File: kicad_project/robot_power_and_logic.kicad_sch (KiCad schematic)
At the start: 17 parts

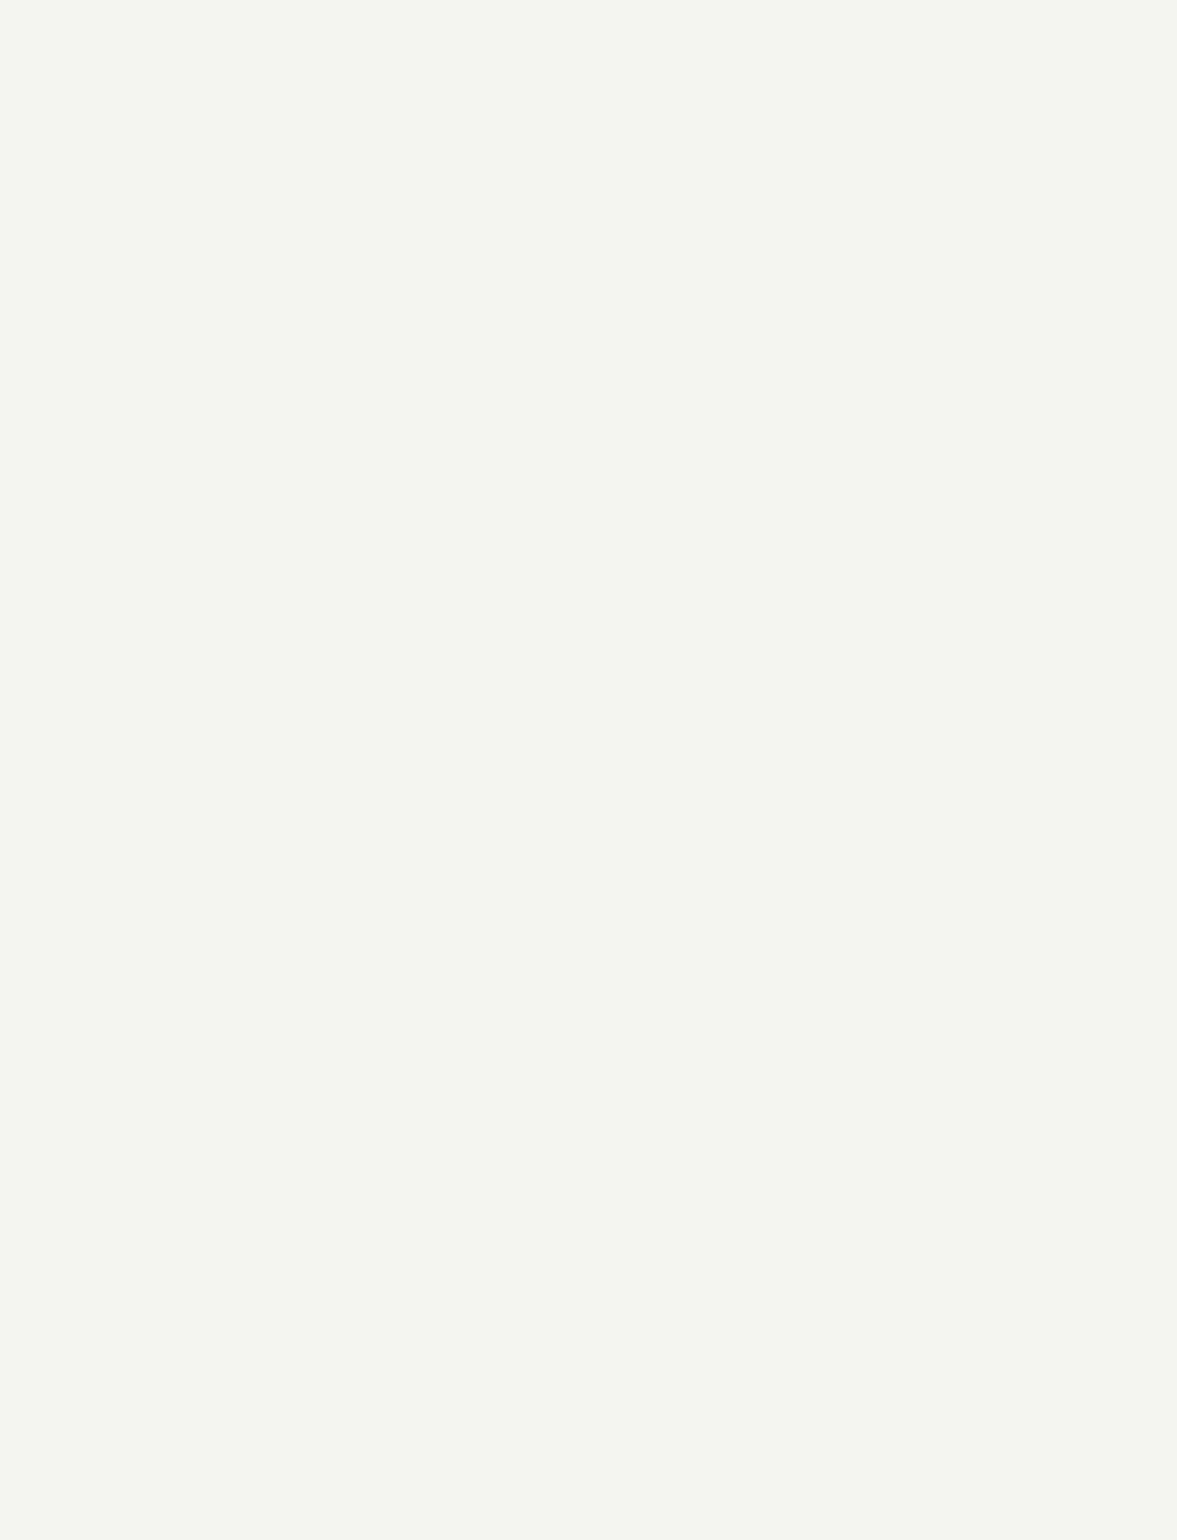
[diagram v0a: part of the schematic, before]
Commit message: Add 2nd motor driver
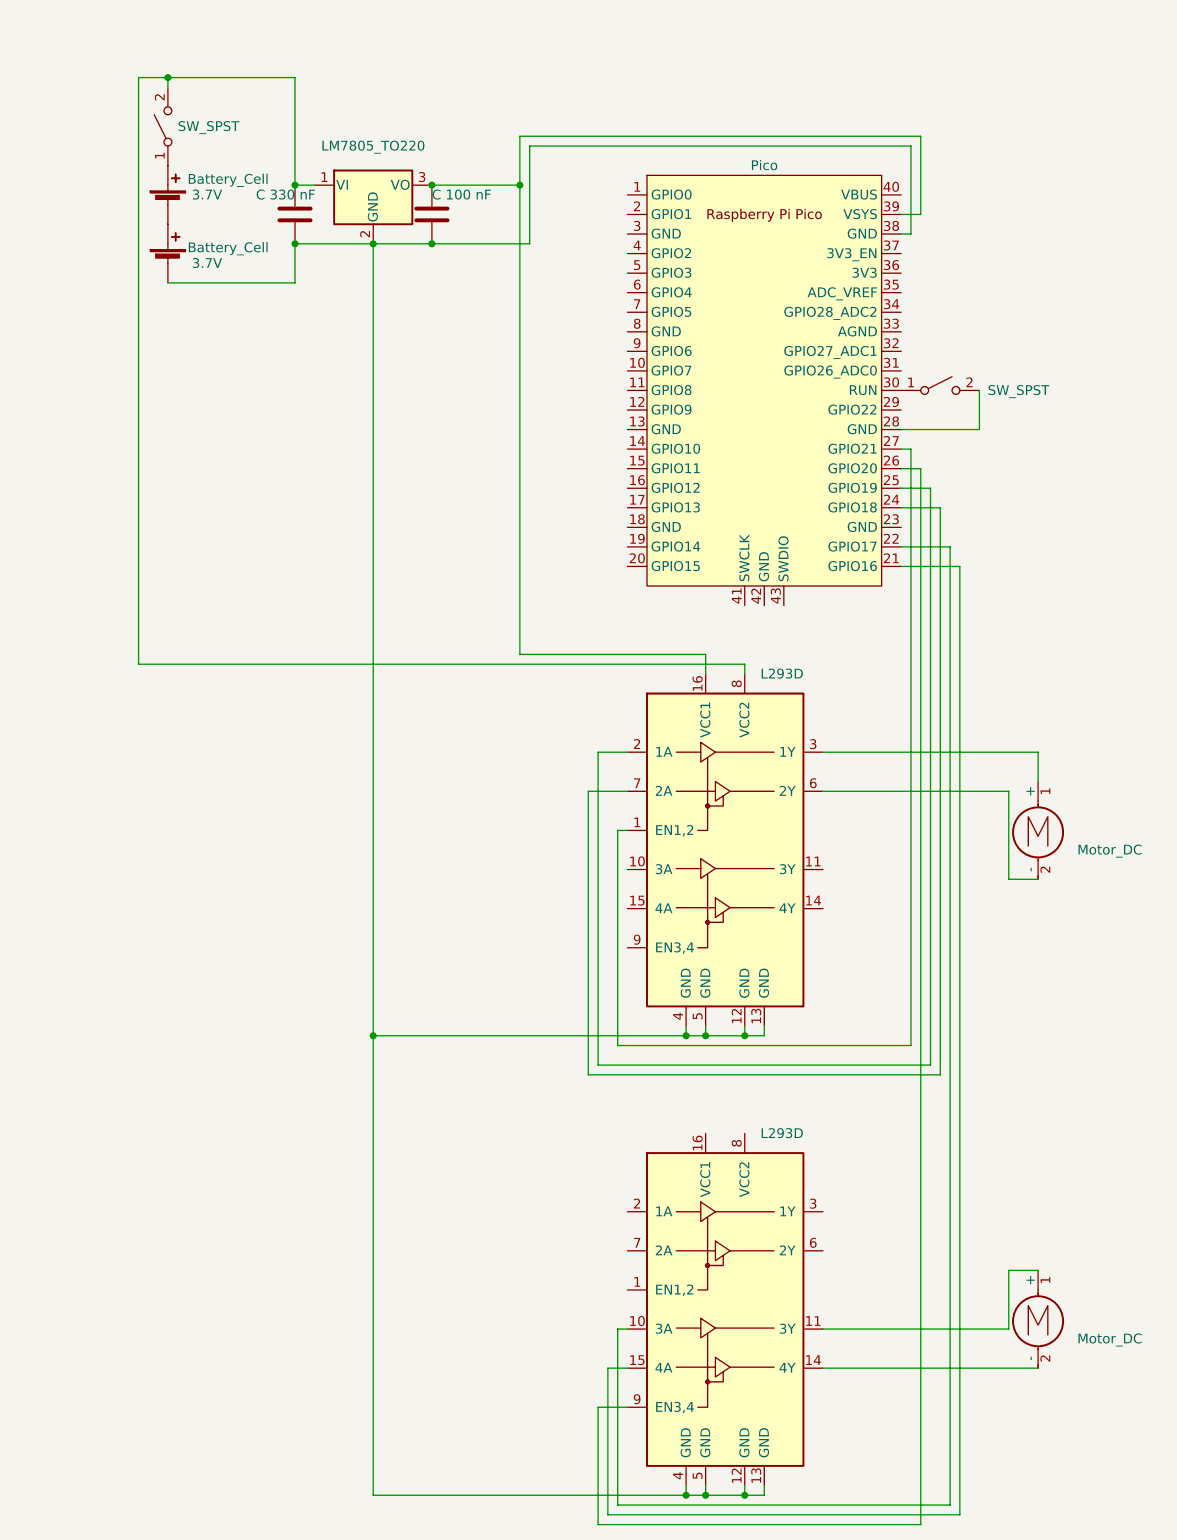
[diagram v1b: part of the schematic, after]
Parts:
- added BT? (x2): Battery_Cell, symbol Device:Battery_Cell
- added C?: C 330 nF, symbol Device:C
- added C?: C 100 nF, symbol Device:C
- added M? (x2): Motor_DC, symbol Motor:Motor_DC
- added SW? (x2): SW_SPST, symbol Switch:SW_SPST
- added U? (x2): L293D, Package_DIP:DIP-16_W7.62mm, symbol Driver_Motor:L293D
- added U?: LM7805_TO220, Package_TO_SOT_THT:TO-220-3_Vertical, symbol Regulator_Linear:LM7805_TO220
- added U?: Pico, RPi_Pico:RPi_Pico_SMD_TH, symbol MCU_RaspberryPi_and_Boards:Pico
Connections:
- new net: BT?.1 (+), SW?.1 (A)
- new net: C?.1, SW?.2 (B), U?.1 (VI), U?.8 (VCC2)
- new net: BT?.1 (+), BT?.2 (-)
- new net: BT?.2 (-), C?.2, C?.2, U?.12 (GND), U?.12 (GND), U?.13 (GND), U?.13 (GND), U?.2 (GND), U?.38 (GND), U?.4 (GND), U?.4 (GND), U?.5 (GND), U?.5 (GND)
- new net: U?.1 (EN1,2), U?.27 (GPIO21)
- new net: C?.1, U?.16 (VCC1), U?.3 (VO), U?.39 (VSYS)
- new net: U?.2 (1A), U?.25 (GPIO19)
- new net: M?.1 (+), U?.3 (1Y)
- new net: M?.2 (-), U?.6 (2Y)
- new net: U?.24 (GPIO18), U?.7 (2A)
- new net: U?.10 (3A), U?.22 (GPIO17)
- new net: M?.1 (+), U?.11 (3Y)
- new net: M?.2 (-), U?.14 (4Y)
- new net: U?.15 (4A), U?.21 (GPIO16)
- new net: U?.26 (GPIO20), U?.9 (EN3,4)
- new net: SW?.2 (B), U?.28 (GND)
- new net: SW?.1 (A), U?.30 (RUN)

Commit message: Remove previous circuit diagrams
cause we have version control for keeping them.
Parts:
- removed BT? (x2): Battery, symbol Device:Battery
- removed C?: C 100 nF, symbol Device:C
- removed C?: C 330 nF, symbol Device:C
- removed M? (x4): Motor_DC, symbol Motor:Motor_DC
- removed SW? (x3): SW_SPST, symbol Switch:SW_SPST
- removed U?: LM7805_TO220, Package_TO_SOT_THT:TO-220-3_Vertical, symbol Regulator_Linear:LM7805_TO220
- removed U? (x2): L293D, Package_DIP:DIP-16_W7.62mm, symbol Driver_Motor:L293D
- removed U?: LM2596T-ADJ, Package_TO_SOT_THT:TO-220-5_P3.4x3.7mm_StaggerOdd_Lead3.8mm_Vertical, symbol Regulator_Switching:LM2596T-ADJ
- removed U? (x2): Pico, RPi_Pico:RPi_Pico_SMD_TH, symbol MCU_RaspberryPi_and_Boards:Pico

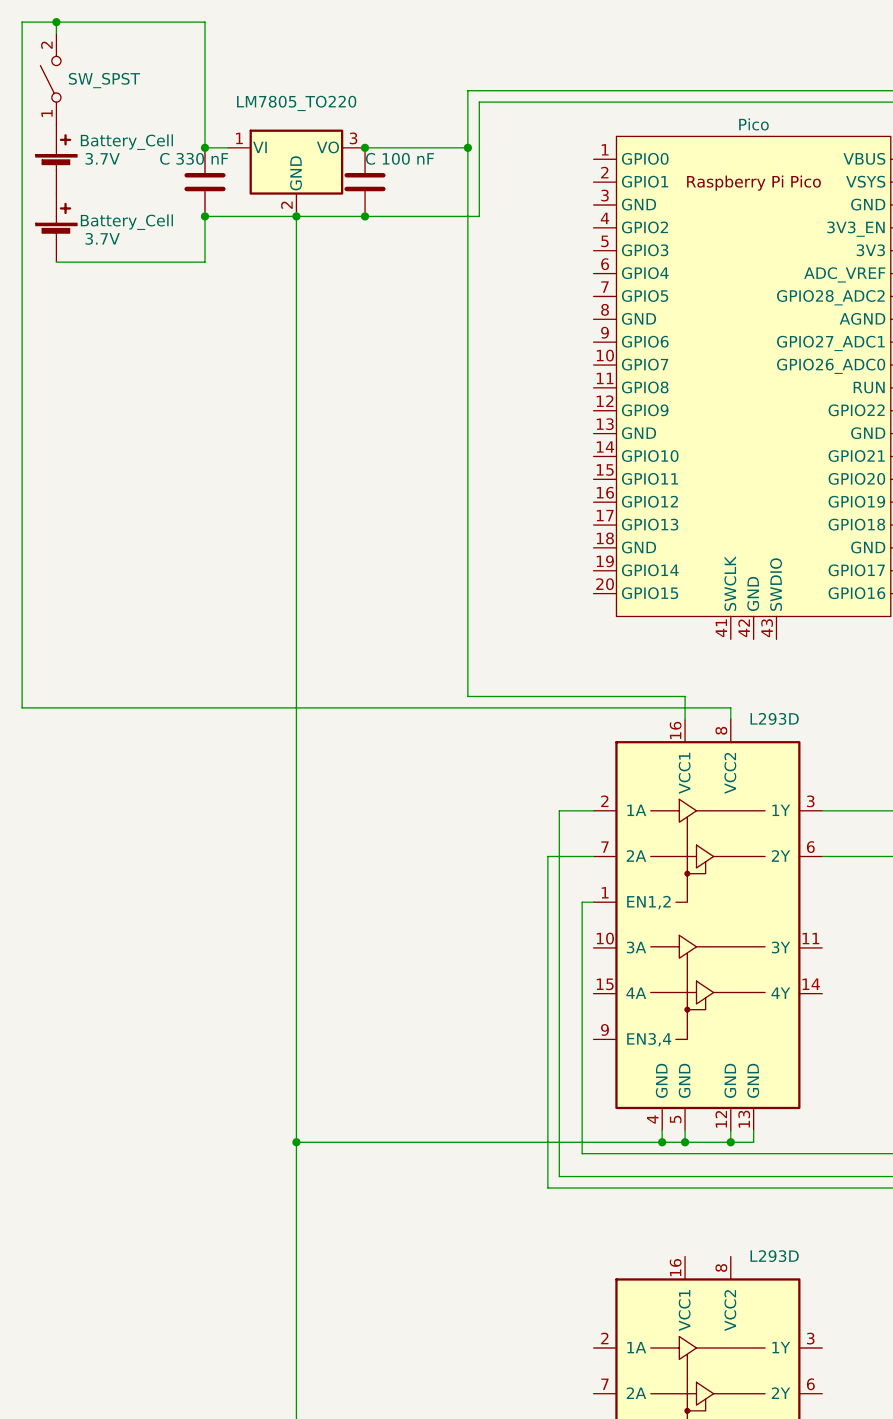
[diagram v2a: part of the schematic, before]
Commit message: Add bypass capacitors to motor drivers
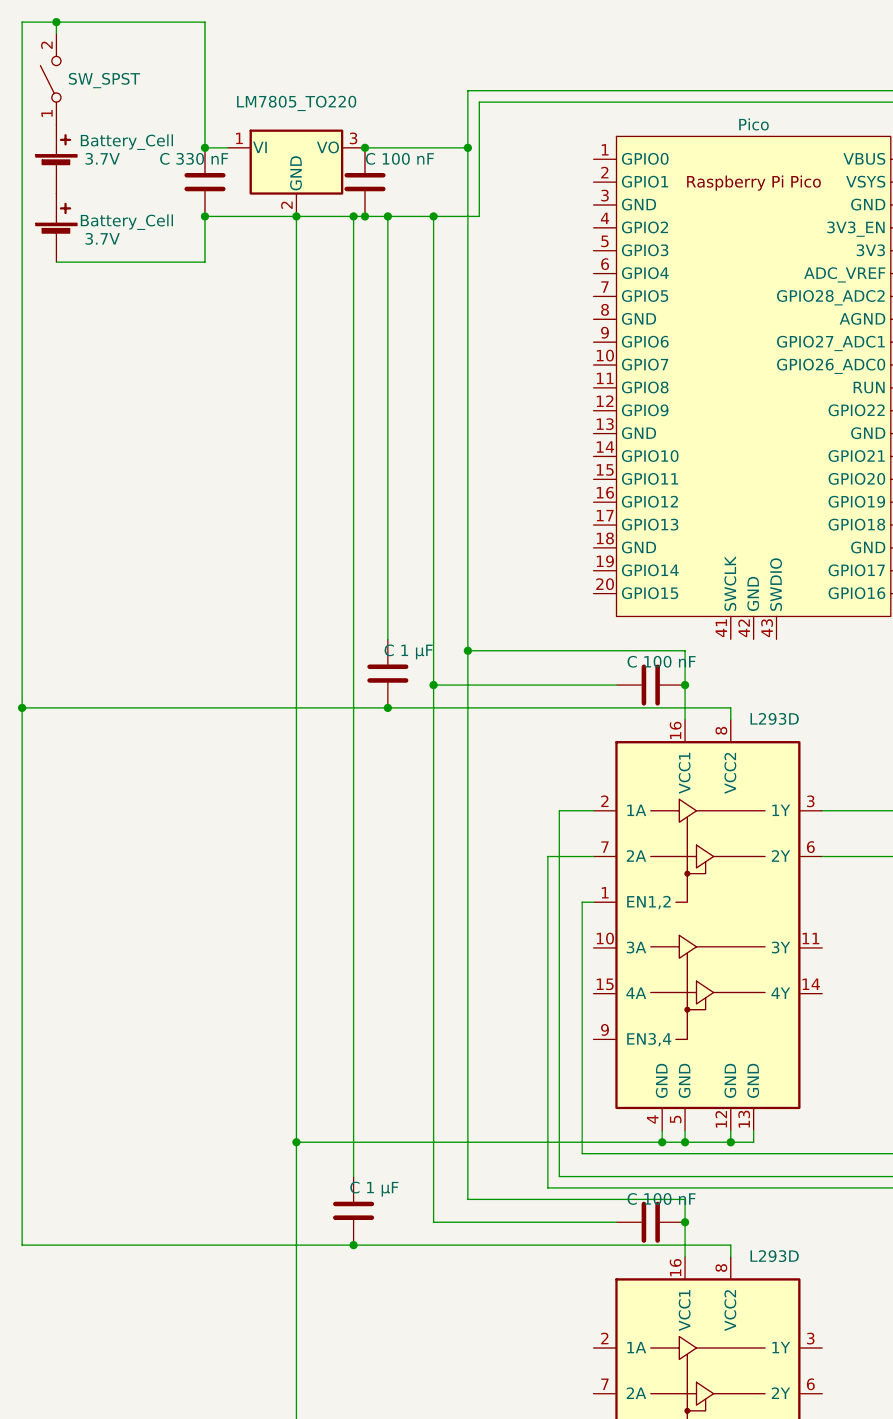
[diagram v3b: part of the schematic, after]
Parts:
- added C? (x2): C 100 nF, symbol Device:C
- added C? (x2): C 1 µF, symbol Device:C
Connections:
- net at C?.1, SW?.2 (B), U?.1 (VI)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: now also U?.8 (VCC2), C?.1, C?.1
- net at BT?.2 (-), C?.2, C?.2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: now also C?.1, C?.1, C?.2, C?.2
- net at C?.1, U?.16 (VCC1), U?.3 (VO)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: now also U?.16 (VCC1), C?.2, C?.2
